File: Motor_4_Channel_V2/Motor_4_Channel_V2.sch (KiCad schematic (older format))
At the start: 54 parts

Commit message: Added power circuit for NRF52. Added SMT Practice V1 project. Modified Motor v2 project.
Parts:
- removed D? (x8): D, symbol Device:D
- removed J? (x4): Conn_01x03_Male, symbol Connector:Conn_01x03_Male
- removed R? (x6): R, symbol Device:R
- removed U?: L7812, symbol Regulator_Linear:L7812
- added C? (x2): 0.33uF, symbol Device:C
- added C? (x3): 0.1uF, symbol Device:C
- added C?: 1nF, symbol Device:C
- added J? (x4): Conn_01x02_Male, symbol Connector:Conn_01x02_Male
- added R? (x2): 47k, Resistor_SMD:R_0603_1608Metric_Pad1.05x0.95mm_HandSolder, symbol Device:R
- added R? (x6): R, Resistor_SMD:R_0603_1608Metric_Pad1.05x0.95mm_HandSolder, symbol Device:R
- added R?: 47K, Resistor_SMD:R_0603_1608Metric_Pad1.05x0.95mm_HandSolder, symbol Device:R
- C?: value C -> 0.1uF
- J? (x2): footprint (none) -> Connector_PinHeader_2.54mm:PinHeader_1x10_P2.54mm_Vertical
- P? (x12): footprint (none) -> Custom_Footprints:Pad
- R? (x3): footprint (none) -> Resistor_SMD:R_0603_1608Metric_Pad1.05x0.95mm_HandSolder
- U?: footprint (none) -> Package_DIP:DIP-20_W7.62mm_Socket_LongPads
- U?: footprint (none) -> Package_TO_SOT_SMD:SOT-223-3_TabPin2
- U? (x4): footprint (none) -> Package_SO:VSSOP-8_2.4x2.1mm_P0.5mm
- U? (x4): footprint (none) -> Custom_Footprints:SC-70-6
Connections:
- wire segments 160 -> 182
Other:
- moved on the sheet: C?, J?, R?, U?

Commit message: Added digikey library. Started PCB layout for Motor 4 CH V2.
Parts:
- C1, C2, C3, C4, C5, C6, C7: renamed from C?; footprint (none) -> Capacitor_SMD:C_0603_1608Metric_Pad1.05x0.95mm_HandSolder
- J1, J10, J2, J3, J4, J5, J6, J7, J9: renamed from J?; footprint (none) -> Connector_PinHeader_2.54mm:PinHeader_1x02_P2.54mm_Vertical
- SW1: renamed from SW?; footprint (none) -> Connector_PinHeader_2.54mm:PinHeader_1x02_P2.54mm_Vertical
- U3: renamed from U?; value AMS1117-5.0 -> UA78M05IDCY
- U4: renamed from U?; value LT1086-3.3 -> UA78M33QDCYRG4Q1
- gave numbers to parts that had none: 35
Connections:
- no-connect marks 44 -> 8
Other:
- moved on the sheet: P1, P10, P11, P12, P2, P3, P4, P5, P6, P7, P8, P9

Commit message: Added progress to Motor 4 CH V2 layout.
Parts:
- U3: symbol Regulator_Linear:AMS1117-5.0 -> Project_Libary:UA78M05IDCY
- U4: symbol Regulator_Linear:LT1086-3.3 -> Project_Libary:UA78M33QDCYRG4Q1
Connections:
- net 12V_REF: now also U3.1 (VI), U4.1 (VI); no longer U3.3 (VI), U4.3 (VI)
- net 3V3_REF: now also U4.3 (VO); no longer U4.2 (VO)
- net 5V_REF: now also U3.3 (VO); no longer U3.2 (VO)
- net BTN_1: now also J8.3 (Pin_3), U11.13 (P2.5); no longer J8.4 (Pin_4), U11.14 (P1.6)
- net BTN_2: now also J11.3 (Pin_3), U11.8 (P2.0); no longer J8.3 (Pin_3), U11.13 (P2.5)
- net BTN_3: now also C7.1, J11.6 (Pin_6), R12.1, U11.5 (P1.3); no longer J8.2 (Pin_2), U11.12 (P2.4)
- net BTN_4: now also J11.9 (Pin_9), U11.2 (P1.0); no longer J8.1 (Pin_1), U11.11 (P2.3)
- net DIR_1: now also J8.2 (Pin_2), U11.12 (P2.4); no longer J11.2 (Pin_2), U11.9 (P2.1)
- net DIR_2: now also J11.2 (Pin_2), U11.9 (P2.1); no longer J11.4 (Pin_4), U11.7 (P1.5)
- net DIR_3: now also J11.5 (Pin_5), U11.6 (P1.4); no longer C7.1, J11.6 (Pin_6), R12.1, U11.5 (P1.3)
- net GND: now also U3.2 (GND), U4.2 (GND); no longer P2.1, U3.1 (GND), U4.1 (GND)
- net GREEN_1: now also J1.1 (Pin_1), R2.1
- net GREEN_2: now also J2.1 (Pin_1), R4.1
- net GREEN_3: now also J7.1 (Pin_1), R6.1
- net GREEN_4: no longer J1.1 (Pin_1), J2.1 (Pin_1), J7.1 (Pin_1), R2.1, R4.1, R6.1
- net OUT_1: now also J8.1 (Pin_1), U11.11 (P2.3); no longer J11.1 (Pin_1), U11.10 (P2.2)
- net OUT_2: now also J11.1 (Pin_1), U11.10 (P2.2); no longer J11.3 (Pin_3), U11.8 (P2.0)
- net OUT_3: now also J11.4 (Pin_4), U11.7 (P1.5); no longer J11.5 (Pin_5), U11.6 (P1.4)
- net RED_1: now also J1.2 (Pin_2), R1.1
- net RED_2: now also J2.2 (Pin_2), R3.1
- net RED_3: now also J7.2 (Pin_2), R5.1
- net RED_4: no longer J1.2 (Pin_2), J2.2 (Pin_2), J7.2 (Pin_2), R1.1, R3.1, R5.1
- new net: J8.4 (Pin_4), U11.14 (P1.6)
- no-connect marks 8 -> 9
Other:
- moved on the sheet: P1, P2
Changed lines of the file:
@@
 $EndComp
 $Comp
-L Regulator_Linear:LT1086-3.3 U4
+L Project_Libary:UA78M33QDCYRG4Q1 U4
 U 1 1 5BEB4959
 P 2900 7400
@@
 L Project_Libary:Pad P1
 U 1 1 5BEBFB70
-P 900 4850
-F 0 "P1" H 999 4896 50  0000 L CNN
-F 1 "Pad" H 999 4805 50  0000 L CNN
-F 2 "Custom_Footprints:Pad" H 900 4850 50  0001 C CNN
-F 3 "" H 900 4850 50  0001 C CNN
-	1    900  4850
+P 800 4800
+F 0 "P1" H 899 4846 50  0000 L CNN
+F 1 "Pad" H 899 4755 50  0000 L CNN
+F 2 "Custom_Footprints:Pad" H 800 4800 50  0001 C CNN
+F 3 "" H 800 4800 50  0001 C CNN
+	1    800  4800
 	0    -1   -1   0
 $EndComp
@@
 L Project_Libary:Pad P2
 U 1 1 5BEBFC75
-P 900 5550
-F 0 "P2" H 999 5596 50  0000 L CNN
-F 1 "Pad" H 999 5505 50  0000 L CNN
-F 2 "Custom_Footprints:Pad" H 900 5550 50  0001 C CNN
-F 3 "" H 900 5550 50  0001 C CNN
-	1    900  5550
+P 800 5550
+F 0 "P2" H 899 5596 50  0000 L CNN
+F 1 "Pad" H 899 5505 50  0000 L CNN
+F 2 "Custom_Footprints:Pad" H 800 5550 50  0001 C CNN
+F 3 "" H 800 5550 50  0001 C CNN
+	1    800  5550
 	0    -1   -1   0
 $EndComp
-Wire Wire Line
-	1100 4850 1450 4850
-Text GLabel 1450 4850 2    50   Output ~ 0
+Text GLabel 1200 4800 2    50   Output ~ 0
 V+
-$Comp
-L power:GND #PWR04
-U 1 1 5BEC2FD4
-P 1550 5600
-F 0 "#PWR04" H 1550 5350 50  0001 C CNN
-F 1 "GND" H 1555 5427 50  0000 C CNN
-F 2 "" H 1550 5600 50  0001 C CNN
-F 3 "" H 1550 5600 50  0001 C CNN
-	1    1550 5600
-	1    0    0    -1
-$EndComp
-Wire Wire Line
-	1550 5550 1550 5600
-Wire Wire Line
-	1100 5550 1550 5550
 Wire Wire Line
 	1850 1400 1450 1400
@@
 Text Notes 650  6850 0    50   ~ 0
 Constant 12VDC\nfrom battery
-Text Notes 600  5300 0    50   ~ 0
+Text Notes 600  5200 0    50   ~ 0
 12V PWM from\npower drill output\n
 Wire Wire Line
@@
 Text GLabel 5925 7475 0    50   Input ~ 0
 BTN_4
-Text GLabel 8750 4700 0    50   Output ~ 0
+Text GLabel 8750 4600 0    50   Output ~ 0
 BTN_1
-Text GLabel 7950 4700 2    50   Input ~ 0
+Text GLabel 7950 4600 2    50   Input ~ 0
 BTN_1
-Text GLabel 8750 4600 0    50   Output ~ 0
+Text GLabel 9650 4600 2    50   Output ~ 0
 BTN_2
-Text GLabel 7950 4600 2    50   Input ~ 0
+Text GLabel 10550 4600 0    50   Input ~ 0
 BTN_2
-Text GLabel 8750 4500 0    50   Output ~ 0
+Text GLabel 9650 4900 2    50   Output ~ 0
 BTN_3
-Text GLabel 7950 4500 2    50   Input ~ 0
+Text GLabel 10550 4900 0    50   Input ~ 0
 BTN_3
-Text GLabel 8750 4400 0    50   Output ~ 0
+Text GLabel 9650 5200 2    50   Output ~ 0
 BTN_4
-Text GLabel 7950 4400 2    50   Input ~ 0
+Text GLabel 10550 5200 0    50   Input ~ 0
 BTN_4
 Wire Wire Line
@@
 	8750 4800 7950 4800
 Connection ~ 10400 5300
+Text GLabel 8750 4400 0    50   Output ~ 0
+OUT_1
+Text GLabel 7950 4400 2    50   Input ~ 0
+OUT_1
 Text GLabel 9650 4400 2    50   Output ~ 0
-OUT_1
+OUT_2
 Text GLabel 10550 4400 0    50   Input ~ 0
-OUT_1
-Text GLabel 9650 4600 2    50   Output ~ 0
 OUT_2
-Text GLabel 10550 4600 0    50   Input ~ 0
-OUT_2
-Text GLabel 9650 4800 2    50   Output ~ 0
+Text GLabel 9650 4700 2    50   Output ~ 0
 OUT_3
-Text GLabel 10550 4800 0    50   Input ~ 0
+Text GLabel 10550 4700 0    50   Input ~ 0
 OUT_3
 Text GLabel 9650 5000 2    50   Output ~ 0
@@
 Text GLabel 10550 5000 0    50   Input ~ 0
 OUT_4
+Text GLabel 7950 4500 2    50   Input ~ 0
+DIR_1
+Text GLabel 8750 4500 0    50   Output ~ 0
+DIR_1
 Text GLabel 10550 4500 0    50   Input ~ 0
-DIR_1
+DIR_2
 Text GLabel 9650 4500 2    50   Output ~ 0
-DIR_1
-Text GLabel 10550 4700 0    50   Input ~ 0
 DIR_2
-Text GLabel 9650 4700 2    50   Output ~ 0
-DIR_2
-Text GLabel 10550 4900 0    50   Input ~ 0
+Text GLabel 10550 4800 0    50   Input ~ 0
 DIR_3
-Text GLabel 9650 4900 2    50   Output ~ 0
+Text GLabel 9650 4800 2    50   Output ~ 0
 DIR_3
 Text GLabel 10550 5100 0    50   Input ~ 0
@@
 $EndComp
 $Comp
-L Regulator_Linear:AMS1117-5.0 U3
+L Project_Libary:UA78M05IDCY U3
 U 1 1 5C1513FD
 P 2900 6700
@@
 	1    0    0    -1
 $EndComp
-Wire Wire Line
-	2900 7000 3050 7000
 Text GLabel 3550 6700 2    50   Output ~ 0
 5V_REF
@@
 	6950 5950 6950 7800
 Wire Notes Line
-	475  4550 1825 4550
-Wire Notes Line
-	1825 4550 1825 5875
-Wire Notes Line
 	4075 5875 4075 7775
 Wire Notes Line
@@
 	2000 6700 2250 6700
 Connection ~ 2250 6700
-Connection ~ 2900 7000
 Wire Wire Line
 	3300 7000 3050 7000
-Connection ~ 3050 7000
 Connection ~ 2900 7700
 Wire Wire Line
@@
 Wire Wire Line
 	2250 7400 2600 7400
-Wire Wire Line
-	2250 7000 2900 7000
 Wire Wire Line
 	2250 6700 2600 6700
@@
 $EndComp
 Text GLabel 5900 2950 0    50   Input ~ 0
-RED_4
+RED_3
 Text GLabel 6400 2950 2    50   Input ~ 0
-GREEN_4
+GREEN_3
 $Comp
 L Connector:Conn_01x02_Male J7
@@
 $EndComp
 Text GLabel 3250 2950 0    50   Input ~ 0
-RED_4
+RED_2
 Text GLabel 3750 2950 2    50   Input ~ 0
-GREEN_4
+GREEN_2
 $Comp
 L Connector:Conn_01x02_Male J2
@@
 $EndComp
 Text GLabel 850  2950 0    50   Input ~ 0
-RED_4
+RED_1
 Text GLabel 1350 2950 2    50   Input ~ 0
-GREEN_4
+GREEN_1
 $Comp
 L Connector:Conn_01x02_Male J1
@@
 	10550 5100 10750 5100
 Wire Wire Line
-	9650 5200 10750 5200
-Wire Wire Line
 	10400 5300 10750 5300
 Wire Wire Line
@@
 	0    1    1    0
 $EndComp
+Wire Wire Line
+	2250 7000 2900 7000
+Connection ~ 3050 7000
+Connection ~ 2900 7000
+Wire Wire Line
+	2900 7000 3050 7000
+Wire Wire Line
+	1000 4800 1200 4800
+Wire Notes Line
+	500  4350 1750 4350
+Wire Notes Line
+	1750 4350 1750 5850
+Wire Wire Line
+	10550 5200 10750 5200
+Wire Wire Line
+	7950 4700 8750 4700
+NoConn ~ 1000 5550
 $EndSCHEMATC

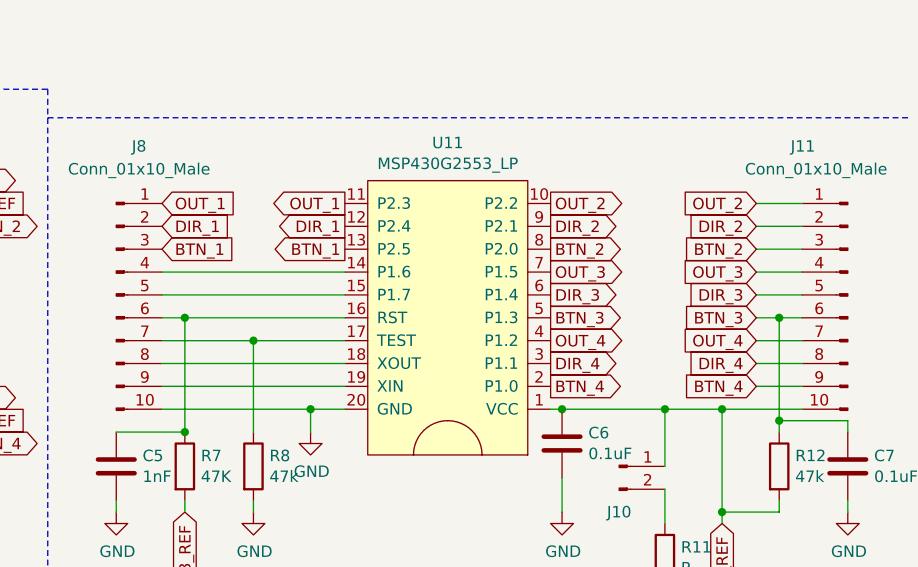
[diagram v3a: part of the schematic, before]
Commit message: Switched THT 2-pin male headers for buttons and led with SMT headers. Rearranged SMT components,
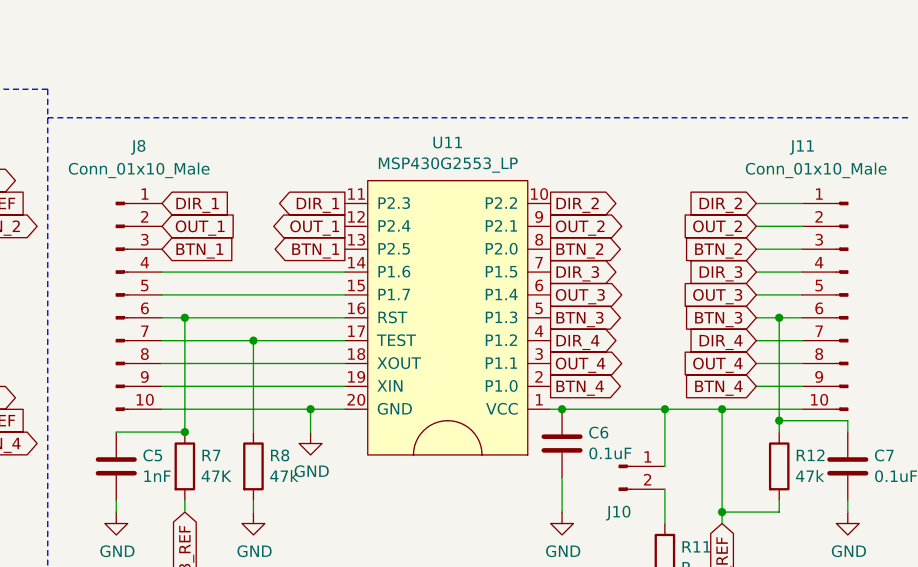
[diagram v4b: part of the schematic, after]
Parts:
- J1, J10, J2, J3, J4, J5, J6, J7, J9: footprint Connector_PinHeader_2.54mm:PinHeader_1x02_P2.54mm_Vertical -> Connector_PinHeader_2.54mm:PinHeader_1x02_P2.54mm_Vertical_SMD_Pin1Left
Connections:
- net DIR_1: now also J8.1 (Pin_1), U11.11 (P2.3); no longer J8.2 (Pin_2), U11.12 (P2.4)
- net DIR_2: now also J11.1 (Pin_1), U11.10 (P2.2); no longer J11.2 (Pin_2), U11.9 (P2.1)
- net DIR_3: now also J11.4 (Pin_4), U11.7 (P1.5); no longer J11.5 (Pin_5), U11.6 (P1.4)
- net DIR_4: now also J11.7 (Pin_7), U11.4 (P1.2); no longer J11.8 (Pin_8), U11.3 (P1.1)
- net OUT_1: now also J8.2 (Pin_2), U11.12 (P2.4); no longer J8.1 (Pin_1), U11.11 (P2.3)
- net OUT_2: now also J11.2 (Pin_2), U11.9 (P2.1); no longer J11.1 (Pin_1), U11.10 (P2.2)
- net OUT_3: now also J11.5 (Pin_5), U11.6 (P1.4); no longer J11.4 (Pin_4), U11.7 (P1.5)
- net OUT_4: now also J11.8 (Pin_8), U11.3 (P1.1); no longer J11.7 (Pin_7), U11.4 (P1.2)
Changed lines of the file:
@@
 F 0 "J10" H 9950 5350 50  0000 C CNN
 F 1 "Conn_01x02_Male" H 9750 5350 50  0001 C CNN
-F 2 "Connector_PinHeader_2.54mm:PinHeader_1x02_P2.54mm_Vertical" H 9950 5550 50  0001 C CNN
+F 2 "Connector_PinHeader_2.54mm:PinHeader_1x02_P2.54mm_Vertical_SMD_Pin1Left" H 9950 5550 50  0001 C CNN
 F 3 "~" H 9950 5550 50  0001 C CNN
 	1    9950 5550
@@
 F 0 "J3" H 4825 6525 50  0000 C CNN
 F 1 "Conn_01x02_Male" H 4775 6425 50  0001 C CNN
-F 2 "Connector_PinHeader_2.54mm:PinHeader_1x02_P2.54mm_Vertical" H 4975 6625 50  0001 C CNN
+F 2 "Connector_PinHeader_2.54mm:PinHeader_1x02_P2.54mm_Vertical_SMD_Pin1Left" H 4975 6625 50  0001 C CNN
 F 3 "~" H 4975 6625 50  0001 C CNN
 	1    4975 6625
@@
 F 0 "J5" H 6025 6525 50  0000 C CNN
 F 1 "Conn_01x02_Male" H 5975 6425 50  0001 C CNN
-F 2 "Connector_PinHeader_2.54mm:PinHeader_1x02_P2.54mm_Vertical" H 6175 6625 50  0001 C CNN
+F 2 "Connector_PinHeader_2.54mm:PinHeader_1x02_P2.54mm_Vertical_SMD_Pin1Left" H 6175 6625 50  0001 C CNN
 F 3 "~" H 6175 6625 50  0001 C CNN
 	1    6175 6625
@@
 F 0 "J4" H 4825 7175 50  0000 C CNN
 F 1 "Conn_01x02_Male" H 4775 7075 50  0001 C CNN
-F 2 "Connector_PinHeader_2.54mm:PinHeader_1x02_P2.54mm_Vertical" H 4975 7275 50  0001 C CNN
+F 2 "Connector_PinHeader_2.54mm:PinHeader_1x02_P2.54mm_Vertical_SMD_Pin1Left" H 4975 7275 50  0001 C CNN
 F 3 "~" H 4975 7275 50  0001 C CNN
 	1    4975 7275
@@
 F 0 "J6" H 6025 7175 50  0000 C CNN
 F 1 "Conn_01x02_Male" H 5975 7075 50  0001 C CNN
-F 2 "Connector_PinHeader_2.54mm:PinHeader_1x02_P2.54mm_Vertical" H 6175 7275 50  0001 C CNN
+F 2 "Connector_PinHeader_2.54mm:PinHeader_1x02_P2.54mm_Vertical_SMD_Pin1Left" H 6175 7275 50  0001 C CNN
 F 3 "~" H 6175 7275 50  0001 C CNN
 	1    6175 7275
@@
 	8750 4800 7950 4800
 Connection ~ 10400 5300
+Text GLabel 8750 4500 0    50   Output ~ 0
+OUT_1
+Text GLabel 7950 4500 2    50   Input ~ 0
+OUT_1
+Text GLabel 9650 4500 2    50   Output ~ 0
+OUT_2
+Text GLabel 10550 4500 0    50   Input ~ 0
+OUT_2
+Text GLabel 9650 4800 2    50   Output ~ 0
+OUT_3
+Text GLabel 10550 4800 0    50   Input ~ 0
+OUT_3
+Text GLabel 9650 5100 2    50   Output ~ 0
+OUT_4
+Text GLabel 10550 5100 0    50   Input ~ 0
+OUT_4
+Text GLabel 7950 4400 2    50   Input ~ 0
+DIR_1
 Text GLabel 8750 4400 0    50   Output ~ 0
-OUT_1
-Text GLabel 7950 4400 2    50   Input ~ 0
-OUT_1
+DIR_1
+Text GLabel 10550 4400 0    50   Input ~ 0
+DIR_2
 Text GLabel 9650 4400 2    50   Output ~ 0
-OUT_2
-Text GLabel 10550 4400 0    50   Input ~ 0
-OUT_2
+DIR_2
+Text GLabel 10550 4700 0    50   Input ~ 0
+DIR_3
 Text GLabel 9650 4700 2    50   Output ~ 0
-OUT_3
-Text GLabel 10550 4700 0    50   Input ~ 0
-OUT_3
+DIR_3
+Text GLabel 10550 5000 0    50   Input ~ 0
+DIR_4
 Text GLabel 9650 5000 2    50   Output ~ 0
-OUT_4
-Text GLabel 10550 5000 0    50   Input ~ 0
-OUT_4
-Text GLabel 7950 4500 2    50   Input ~ 0
-DIR_1
-Text GLabel 8750 4500 0    50   Output ~ 0
-DIR_1
-Text GLabel 10550 4500 0    50   Input ~ 0
-DIR_2
-Text GLabel 9650 4500 2    50   Output ~ 0
-DIR_2
-Text GLabel 10550 4800 0    50   Input ~ 0
-DIR_3
-Text GLabel 9650 4800 2    50   Output ~ 0
-DIR_3
-Text GLabel 10550 5100 0    50   Input ~ 0
-DIR_4
-Text GLabel 9650 5100 2    50   Output ~ 0
 DIR_4
 Text GLabel 1850 2950 3    50   Input ~ 0
@@
 F 0 "J9" V 8750 2850 50  0000 C CNN
 F 1 "Conn_01x02_Male" H 8500 2550 50  0001 C CNN
-F 2 "Connector_PinHeader_2.54mm:PinHeader_1x02_P2.54mm_Vertical" H 8700 2750 50  0001 C CNN
+F 2 "Connector_PinHeader_2.54mm:PinHeader_1x02_P2.54mm_Vertical_SMD_Pin1Left" H 8700 2750 50  0001 C CNN
 F 3 "~" H 8700 2750 50  0001 C CNN
 	1    8700 2750
@@
 F 0 "J7" V 6250 2850 50  0000 C CNN
 F 1 "Conn_01x02_Male" H 6000 2550 50  0001 C CNN
-F 2 "Connector_PinHeader_2.54mm:PinHeader_1x02_P2.54mm_Vertical" H 6200 2750 50  0001 C CNN
+F 2 "Connector_PinHeader_2.54mm:PinHeader_1x02_P2.54mm_Vertical_SMD_Pin1Left" H 6200 2750 50  0001 C CNN
 F 3 "~" H 6200 2750 50  0001 C CNN
 	1    6200 2750
@@
 F 0 "J2" V 3600 2850 50  0000 C CNN
 F 1 "Conn_01x02_Male" H 3350 2550 50  0001 C CNN
-F 2 "Connector_PinHeader_2.54mm:PinHeader_1x02_P2.54mm_Vertical" H 3550 2750 50  0001 C CNN
+F 2 "Connector_PinHeader_2.54mm:PinHeader_1x02_P2.54mm_Vertical_SMD_Pin1Left" H 3550 2750 50  0001 C CNN
 F 3 "~" H 3550 2750 50  0001 C CNN
 	1    3550 2750
@@
 F 0 "J1" V 1200 2850 50  0000 C CNN
 F 1 "Conn_01x02_Male" H 950 2550 50  0001 C CNN
-F 2 "Connector_PinHeader_2.54mm:PinHeader_1x02_P2.54mm_Vertical" H 1150 2750 50  0001 C CNN
+F 2 "Connector_PinHeader_2.54mm:PinHeader_1x02_P2.54mm_Vertical_SMD_Pin1Left" H 1150 2750 50  0001 C CNN
 F 3 "~" H 1150 2750 50  0001 C CNN
 	1    1150 2750

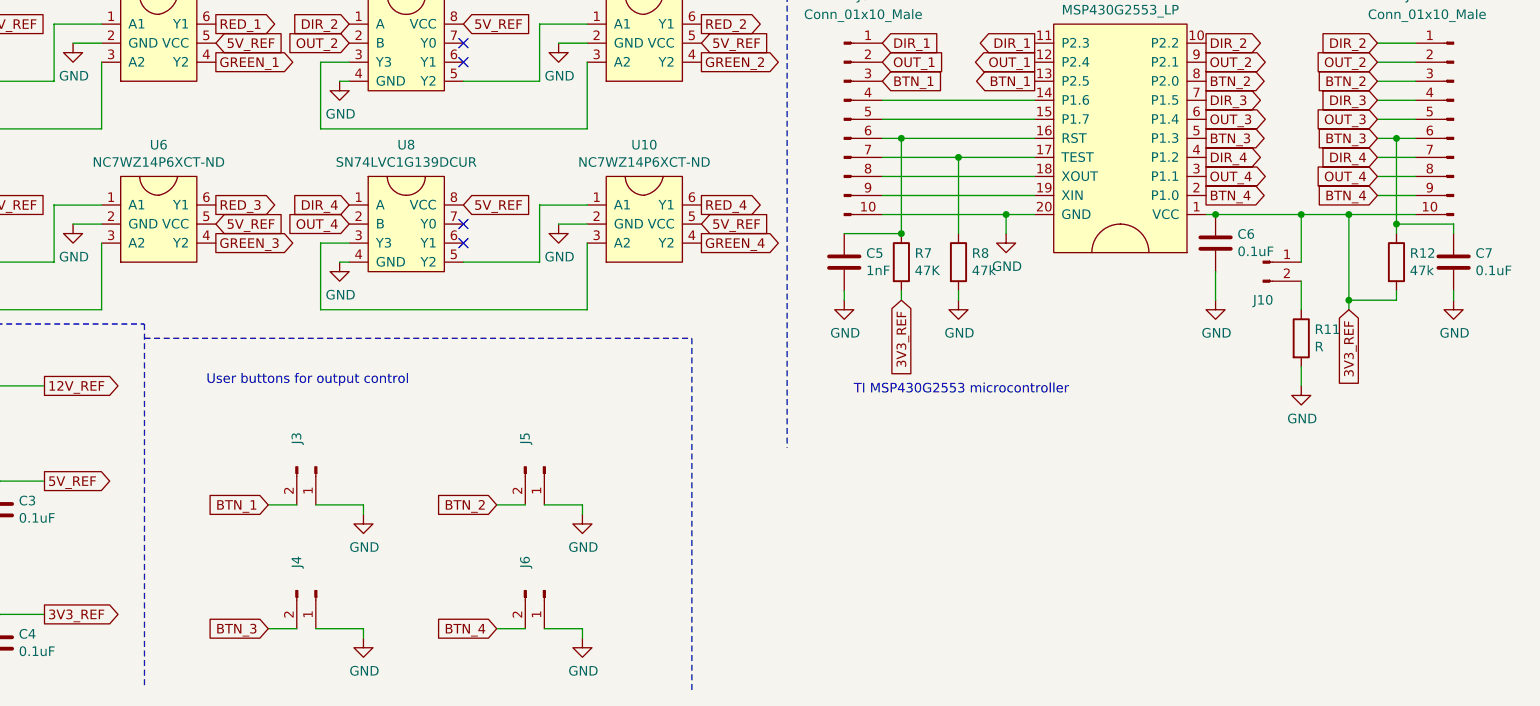
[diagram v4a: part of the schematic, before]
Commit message: Added RC circuit to each button for hardware debouncing.
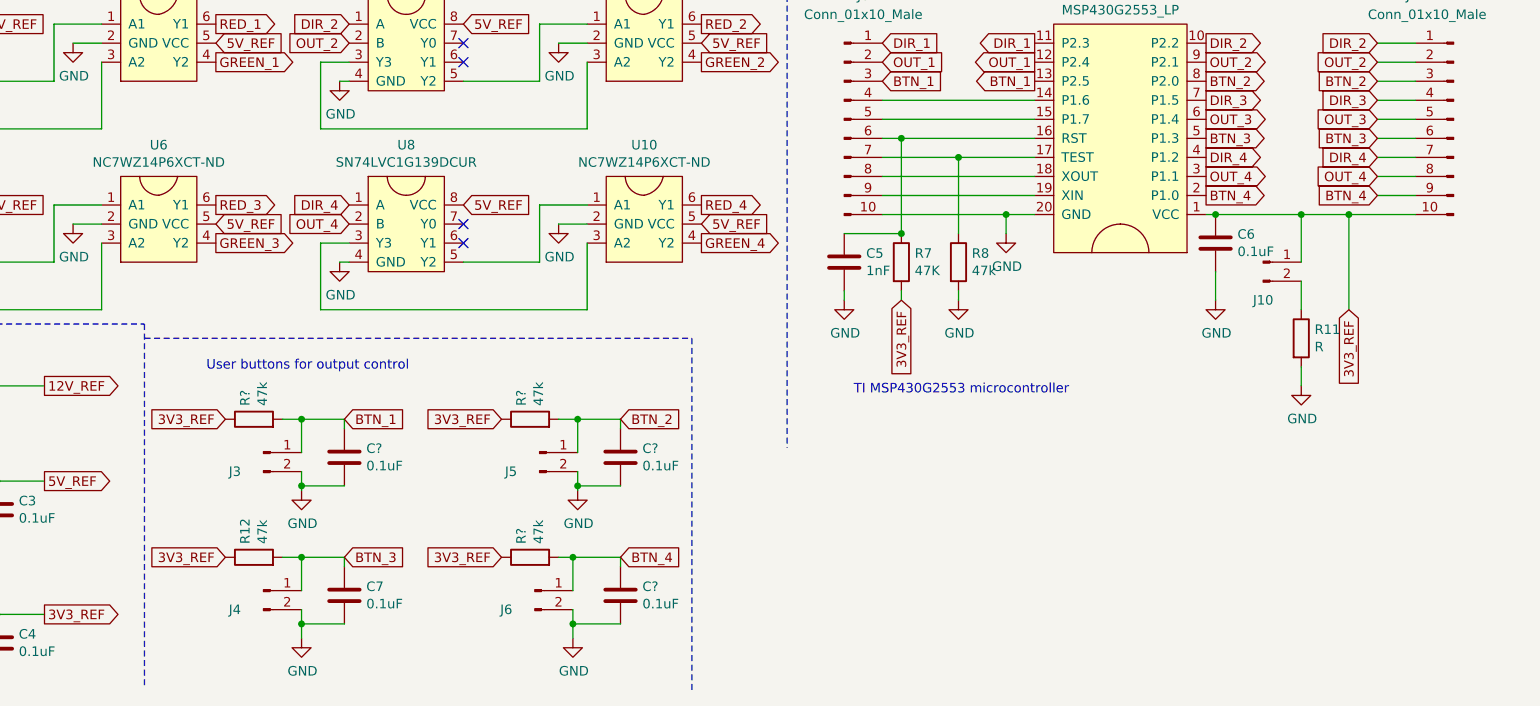
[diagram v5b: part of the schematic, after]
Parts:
- added C? (x3): 0.1uF, Capacitor_SMD:C_0603_1608Metric_Pad1.05x0.95mm_HandSolder, symbol Device:C
- added R? (x3): 47k, Resistor_SMD:R_0603_1608Metric_Pad1.05x0.95mm_HandSolder, symbol Device:R
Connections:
- net 3V3_REF: now also R12.1, R?.1, R?.1, R?.1; no longer R12.2
- net BTN_1: now also J3.1 (Pin_1), C?.1, R?.2; no longer J3.2 (Pin_2)
- net BTN_2: now also J5.1 (Pin_1), C?.1, R?.2; no longer J5.2 (Pin_2)
- net BTN_3: now also J4.1 (Pin_1), R12.2; no longer J4.2 (Pin_2), R12.1
- net BTN_4: now also J6.1 (Pin_1), C?.1, R?.2; no longer J6.2 (Pin_2)
- net GND: now also J3.2 (Pin_2), J4.2 (Pin_2), J5.2 (Pin_2), J6.2 (Pin_2), C?.2, C?.2, C?.2; no longer J3.1 (Pin_1), J4.1 (Pin_1), J5.1 (Pin_1), J6.1 (Pin_1)
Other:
- moved on the sheet: C7, J3, J4, J5, J6, R12
